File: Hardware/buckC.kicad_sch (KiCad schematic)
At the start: 20 parts, among them U6 SiC437BED-T1-GE3

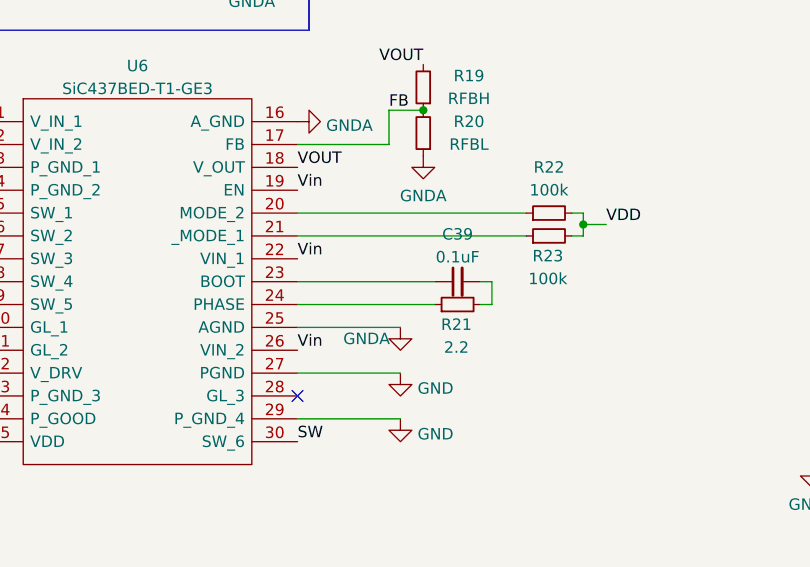
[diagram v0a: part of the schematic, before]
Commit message: initial layout for rough sizing
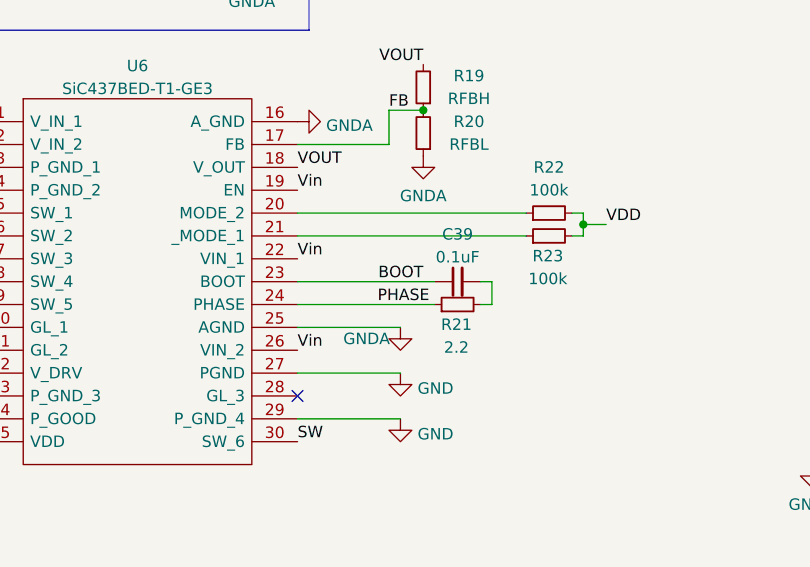
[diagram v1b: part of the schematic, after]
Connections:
- net BOOT: now reaches C39.1, U6.23 (BOOT)
- net PHASE: now reaches R21.1, U6.24 (PHASE)
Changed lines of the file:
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@@
     (effects (font (size 1.27 1.27)) (justify right bottom))
+  )
+  (label "PHASE" (at 119.38 71.12 0)
+    (effects (font (size 1.27 1.27)) (justify left bottom))
   )
   (label "VOUT" (at 58.42 66.04 180)
@@
     (effects (font (size 1.27 1.27)) (justify left bottom))
   )
+  (label "BOOT" (at 124.46 68.58 180)
+    (effects (font (size 1.27 1.27)) (justify right bottom))
+  )
   (label "SW" (at 110.49 86.36 0)

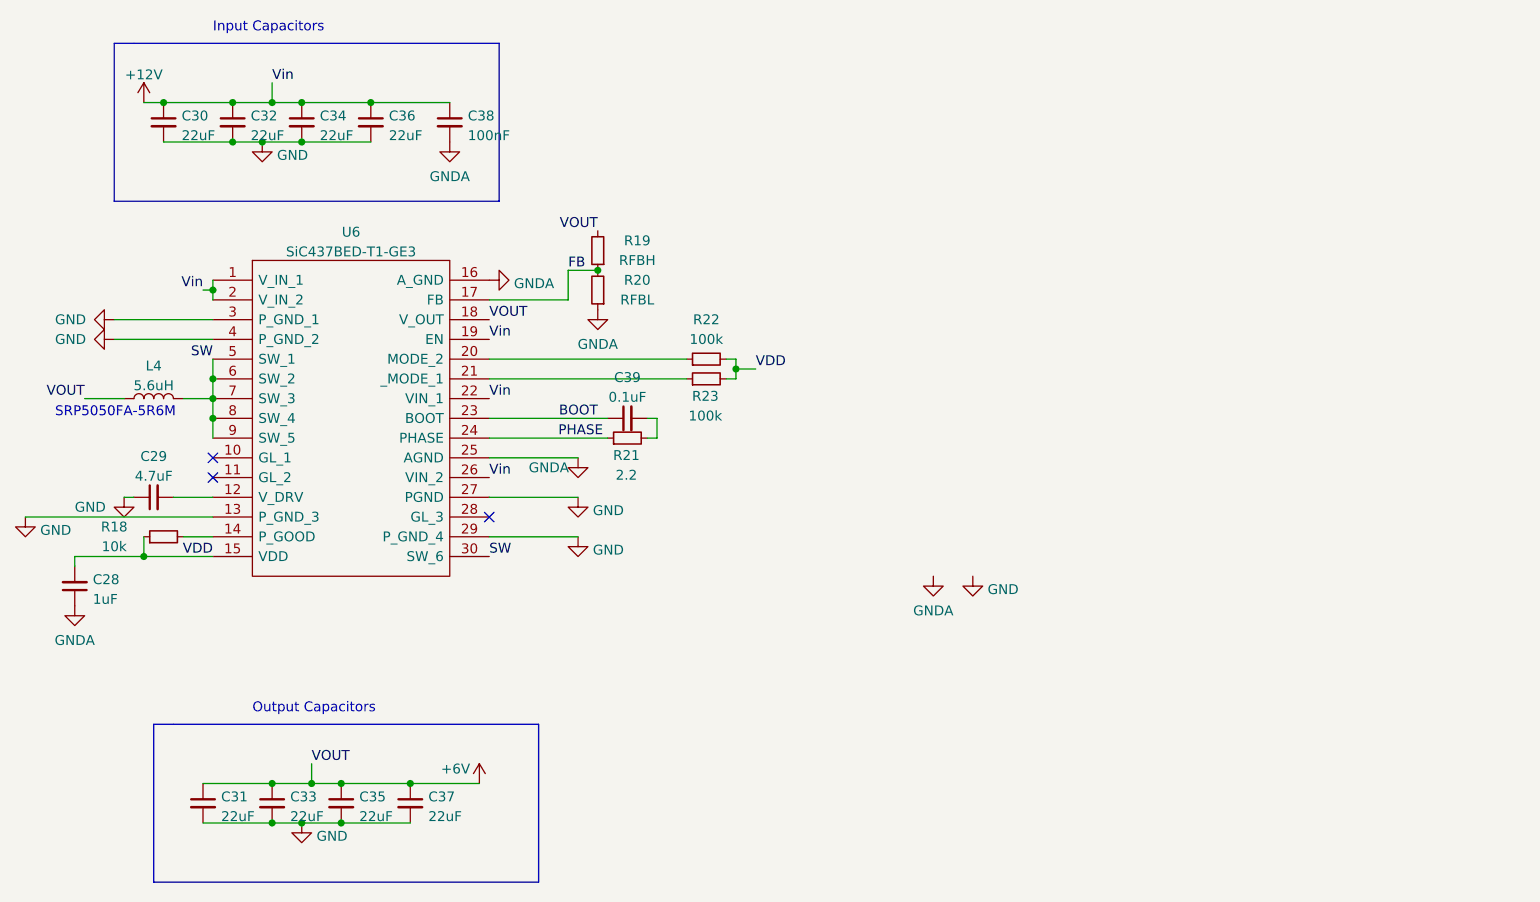
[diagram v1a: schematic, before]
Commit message: on the verge of being complete, also updated to kicad 7
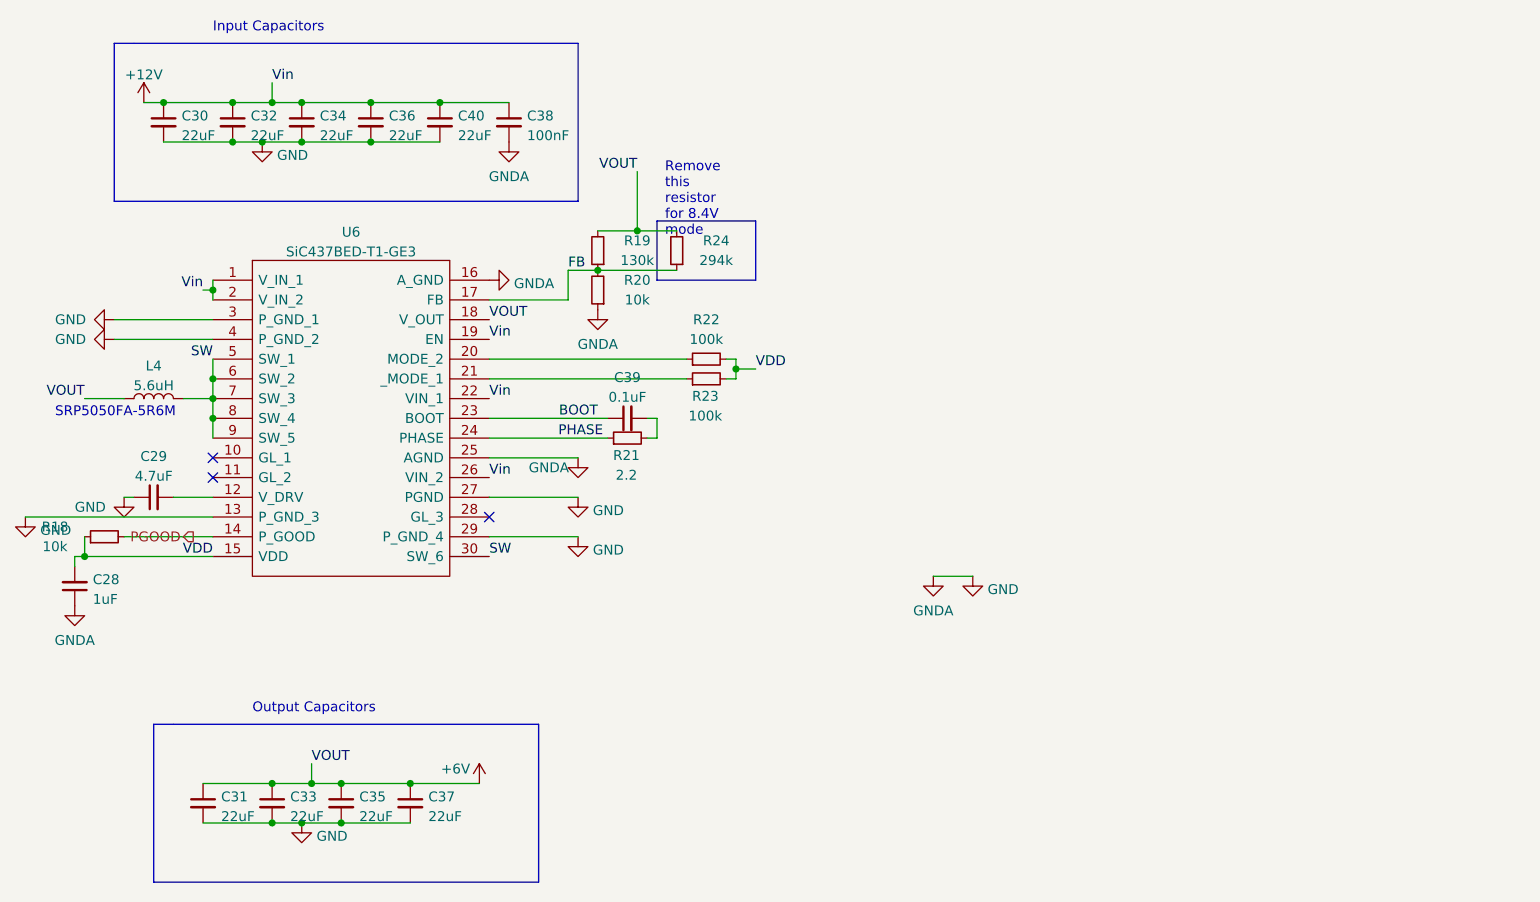
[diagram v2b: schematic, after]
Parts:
- added C40: 22uF, Capacitor_SMD:C_0805_2012Metric, symbol Device:C_Small
- added R24: 294k, Capacitor_SMD:C_0402_1005Metric, symbol Device:R_Small
- R19: value RFBH -> 130k
- R20: value RFBL -> 10k
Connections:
- net GNDA is gone; now on net GND: C28.1, C38.2, R20.1, U6.16 (A_GND), U6.25 (AGND)
- net +12V: now also C40.1
- net +6V: now also R24.2
- net FB: now also R24.1
- net GND: now also C40.2
- net PGOOD: now reaches R18.2, U6.14 (P_GOOD)
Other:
- moved on the sheet: C38, R18

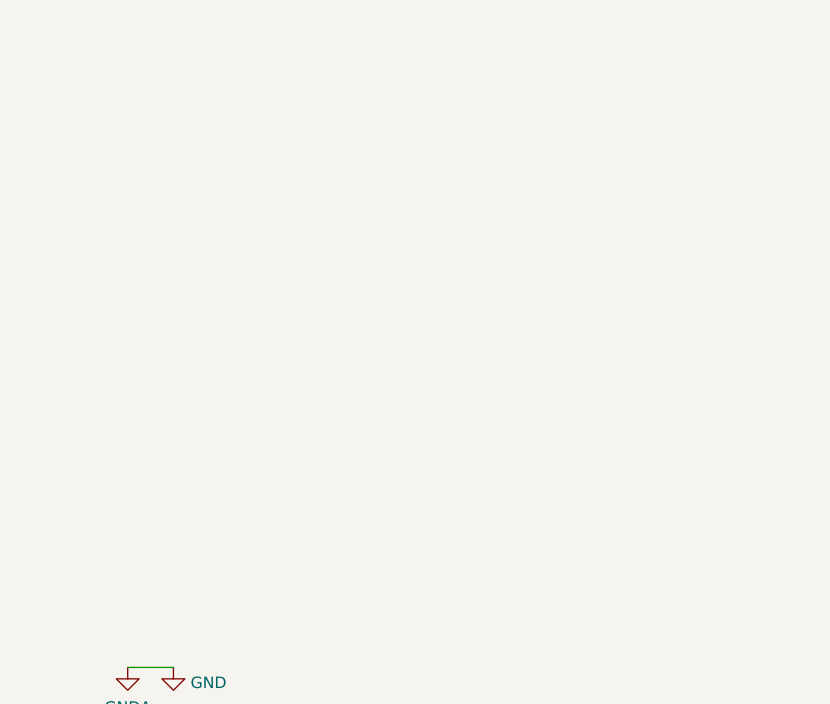
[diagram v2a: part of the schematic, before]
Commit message: added DNP capacitors, via fencing. still left: reduce number of vias
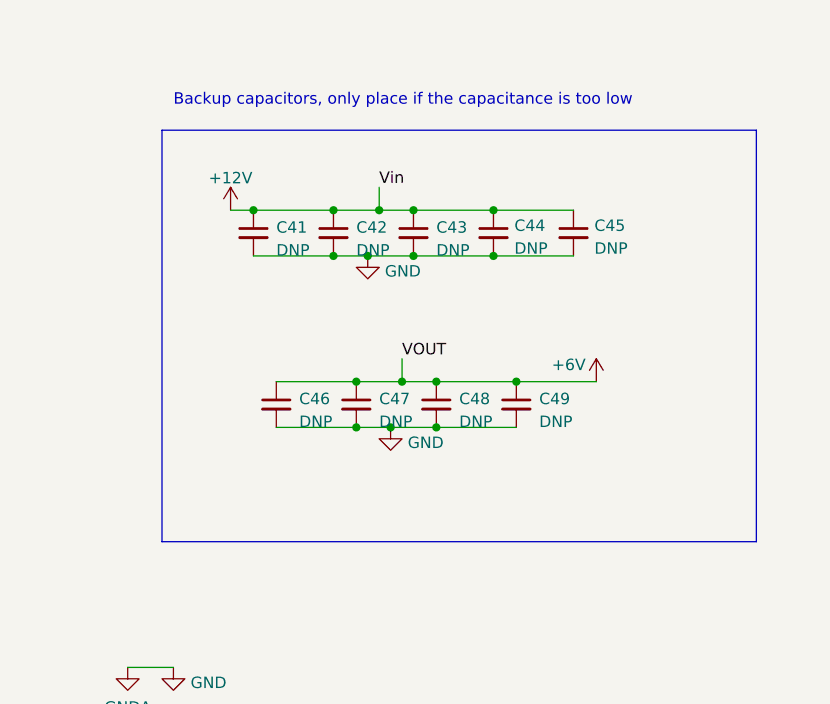
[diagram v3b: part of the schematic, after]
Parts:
- added C41, C42, C43, C44, C45, C46, C47, C48, C49: DNP, Capacitor_SMD:C_0805_2012Metric, symbol Device:C_Small
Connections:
- net +12V: now also C41.1, C42.1, C43.1, C44.1, C45.1
- net +6V: now also C46.1, C47.1, C48.1, C49.1
- net GND: now also C41.2, C42.2, C43.2, C44.2, C45.2, C46.2, C47.2, C48.2, C49.2
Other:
- note added: "Backup capacitors, only place if the capacitance is too low"

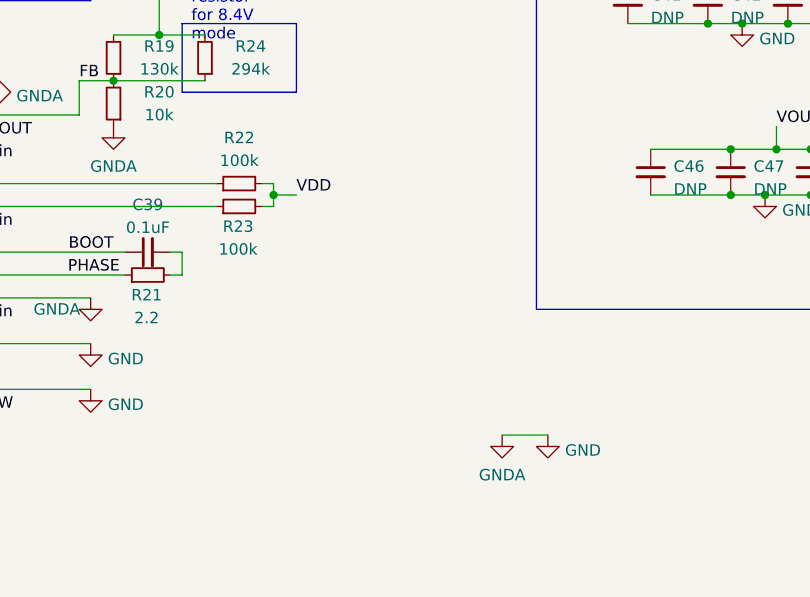
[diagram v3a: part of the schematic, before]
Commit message: fixed via numbers, added gpio pullup option, need to decide PGood flag
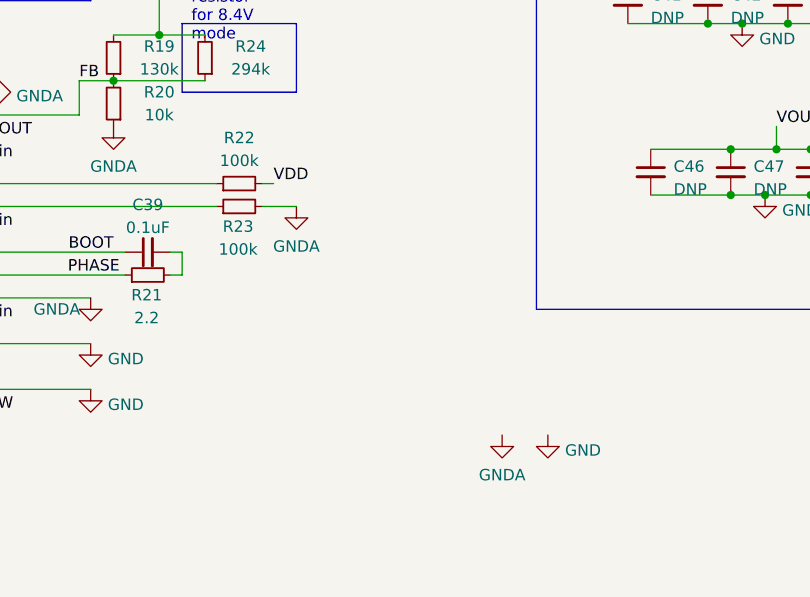
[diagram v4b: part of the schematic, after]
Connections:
- net GND: no longer C28.1, C38.2, R20.1, U6.16 (A_GND), U6.25 (AGND)
- net VDD: no longer R23.2
- new net GNDA: C28.1, C38.2, R20.1, R23.2, U6.16 (A_GND), U6.25 (AGND)
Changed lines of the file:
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@@
   (junction (at 77.47 27.94) (diameter 0) (color 0 0 0 0)
-  )
-  (junction (at 142.24 62.23) (diameter 0) (color 0 0 0 0)
   )
   (junction (at 87.63 115.57) (diameter 0) (color 0 0 0 0)
@@
     (stroke (width 0) (type default))
   )
-  (wire (pts (xy 140.97 63.5) (xy 142.24 63.5))
+  (wire (pts (xy 140.97 63.5) (xy 144.78 63.5))
     (stroke (width 0) (type default))
   )
@@
     (stroke (width 0) (type default))
   )
-  (wire (pts (xy 142.24 62.23) (xy 144.78 62.23))
-    (stroke (width 0) (type default))
-  )
   (wire (pts (xy 87.63 115.57) (xy 91.44 115.57))
     (stroke (width 0) (type default))
@@
     (stroke (width 0) (type default))
   )
-  (wire (pts (xy 167.64 88.9) (xy 172.72 88.9))
-    (stroke (width 0) (type default))
-  )
   (wire (pts (xy 68.58 33.02) (xy 77.47 33.02))
     (stroke (width 0) (type default))
@@
     (stroke (width 0) (type default))
   )
-  (wire (pts (xy 142.24 60.96) (xy 142.24 62.23))
-    (stroke (width 0) (type default))
-  )
   (wire (pts (xy 193.04 62.23) (xy 196.85 62.23))
     (stroke (width 0) (type default))
   )
   (wire (pts (xy 86.36 120.65) (xy 91.44 120.65))
-    (stroke (width 0) (type default))
-  )
-  (wire (pts (xy 142.24 62.23) (xy 142.24 63.5))
     (stroke (width 0) (type default))
   )
@@
     (effects (font (size 1.27 1.27)) (justify left bottom))
   )
-  (label "VDD" (at 144.78 62.23 0) (fields_autoplaced)
+  (label "VDD" (at 142.24 60.96 0) (fields_autoplaced)
     (effects (font (size 1.27 1.27)) (justify left bottom))
   )
@@
         )
       )
+    )
+  )
+  (symbol (lib_id "power:GNDA") (at 144.78 63.5 0) (unit 1)
+    (in_bom yes) (on_board yes) (dnp no) (fields_autoplaced)
+    (property "Reference" "#PWR080" (at 144.78 69.85 0)
+      (effects (font (size 1.27 1.27)) hide)
+    )
+    (property "Value" "GNDA" (at 144.78 67.9434 0)
+      (effects (font (size 1.27 1.27)))
+    )
+    (property "Footprint" "" (at 144.78 63.5 0)
+      (effects (font (size 1.27 1.27)) hide)
+    )
+    (property "Datasheet" "" (at 144.78 63.5 0)
+      (effects (font (size 1.27 1.27)) hide)
+    )
+    (pin "1")
+    (instances
+      (project "Chad"
+        (path "/7db990e4-92e1-4f99-b4d2-435bbec1ba83/8734796e-d088-404b-9453-b276f910a8bb"
+          (reference "#PWR080") (unit 1)
+        )
+      )

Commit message: v2 finished? (pre-review)
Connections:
- net GNDA is gone; now on net GND: C28.1, C38.2, R20.1, R23.2, U6.16 (A_GND), U6.25 (AGND)
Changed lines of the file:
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@@
+    (stroke (width 0) (type default))
+  )
+  (wire (pts (xy 167.64 88.9) (xy 172.72 88.9))
     (stroke (width 0) (type default))
   )
@@
     )
   )
-  (symbol (lib_id "power:GNDA") (at 167.64 88.9 0) (unit 1)
-    (in_bom yes) (on_board yes) (dnp no) (fields_autoplaced)
+  (symbol (lib_id "power:GNDA") (at 167.64 88.9 0) (mirror y) (unit 1)
+    (in_bom yes) (on_board yes) (dnp no)
     (property "Reference" "#PWR072" (at 167.64 95.25 0)
       (effects (font (size 1.27 1.27)) hide)
@@
   (symbol (lib_id "Device:R_Small") (at 60.96 83.82 90) (unit 1)
     (in_bom yes) (on_board yes) (dnp no)
-    (property "Reference" "R18" (at 54.61 82.55 90)
-      (effects (font (size 1.27 1.27)))
-    )
+    (property "Reference" "R18" (at 60.96 82.55 90)
+      (effects (font (size 1.27 1.27)))
+    )

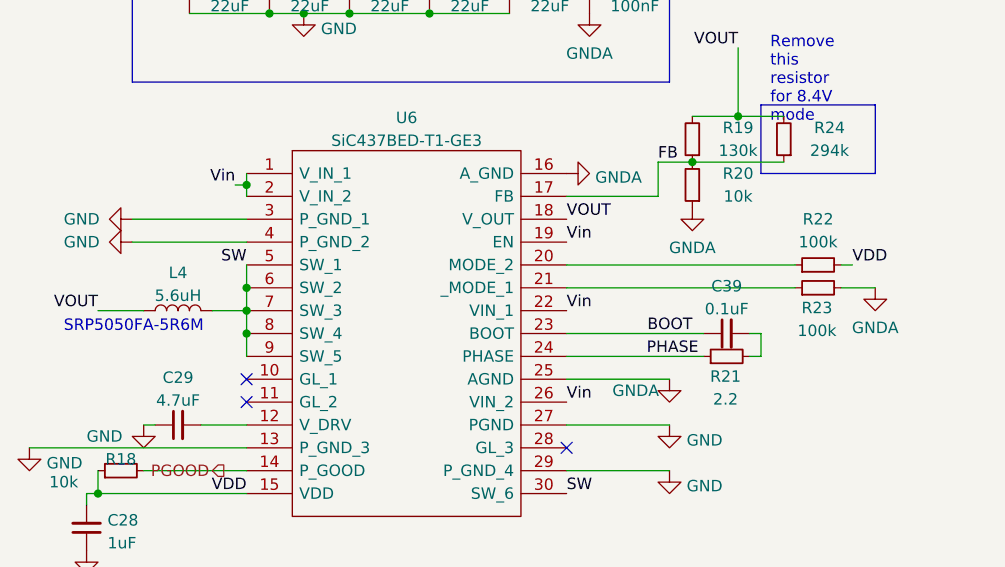
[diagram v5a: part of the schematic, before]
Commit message: updated current limit resistor (oops)
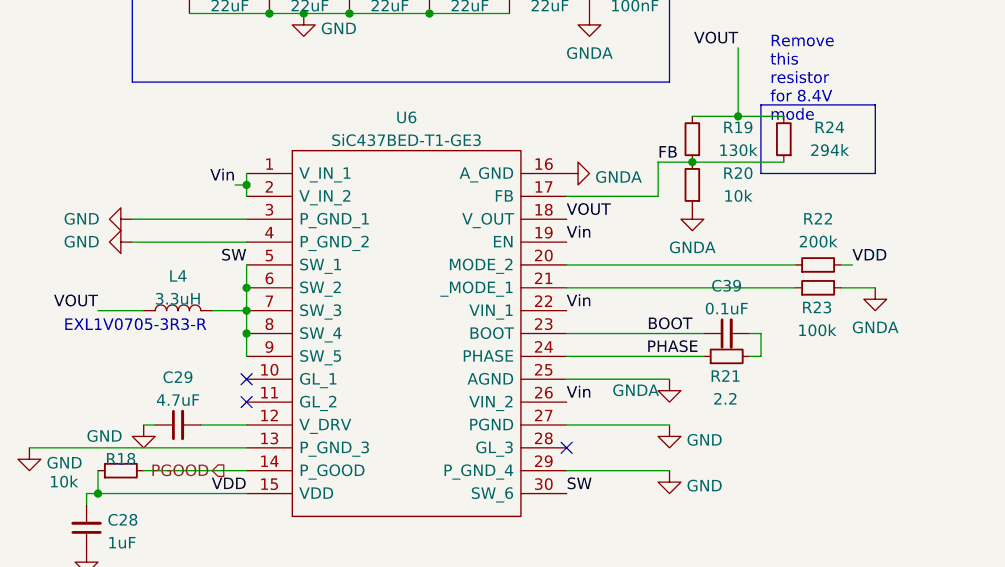
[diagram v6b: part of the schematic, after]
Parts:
- L4: value 5.6uH -> 3.3uH; footprint iclr:SRP5050FA5R6M -> iclr:EXL1V07053R3R
- R22: value 100k -> 200k
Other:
- note added: "EXL1V0705-3R3-R"
- note removed: "SRP5050FA-5R6M"
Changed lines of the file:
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@@
     (effects (font (size 1.27 1.27)) (justify left bottom))
   )
-  (text "SRP5050FA-5R6M" (at 54.61 68.58 0)
+  (text "EXL1V0705-3R3-R" (at 54.61 68.58 0)
     (effects (font (size 1.27 1.27)) (justify left bottom))
   )
@@
   (symbol (lib_id "Device:L") (at 67.31 66.04 90) (unit 1)
     (in_bom yes) (on_board yes) (dnp no) (fields_autoplaced)
-    (property "Reference" "L4" (at 67.31 61.8322 90)
-      (effects (font (size 1.27 1.27)))
-    )
-    (property "Value" "5.6uH" (at 67.31 64.3691 90)
-      (effects (font (size 1.27 1.27)))
-    )
-    (property "Footprint" "iclr:SRP5050FA5R6M" (at 67.31 66.04 0)
+    (property "Reference" "L4" (at 67.31 62.23 90)
+      (effects (font (size 1.27 1.27)))
+    )
+    (property "Value" "3.3uH" (at 67.31 64.77 90)
+      (effects (font (size 1.27 1.27)))
+    )
+    (property "Footprint" "iclr:EXL1V07053R3R" (at 67.31 66.04 0)
       (effects (font (size 1.27 1.27)) hide)
     )
@@
       (effects (font (size 1.27 1.27)))
     )
-    (property "Value" "100k" (at 138.43 58.4169 90)
-      (effects (font (size 1.27 1.27)))
-    )
+    (property "Value" "200k" (at 138.43 58.4169 90)
+      (effects (font (size 1.27 1.27)))
+    )
